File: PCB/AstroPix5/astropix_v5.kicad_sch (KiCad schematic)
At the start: 40 parts, among them J1 HBOut, J12 Measures_Analog, J13 pcie_GECCO, J14 Bias, J2 Conn_01x05, J4 HBOut, J5 HBOut, J7 HV_in_external, J8 Conn_01x03, U2 AstroPix5_split_powerring

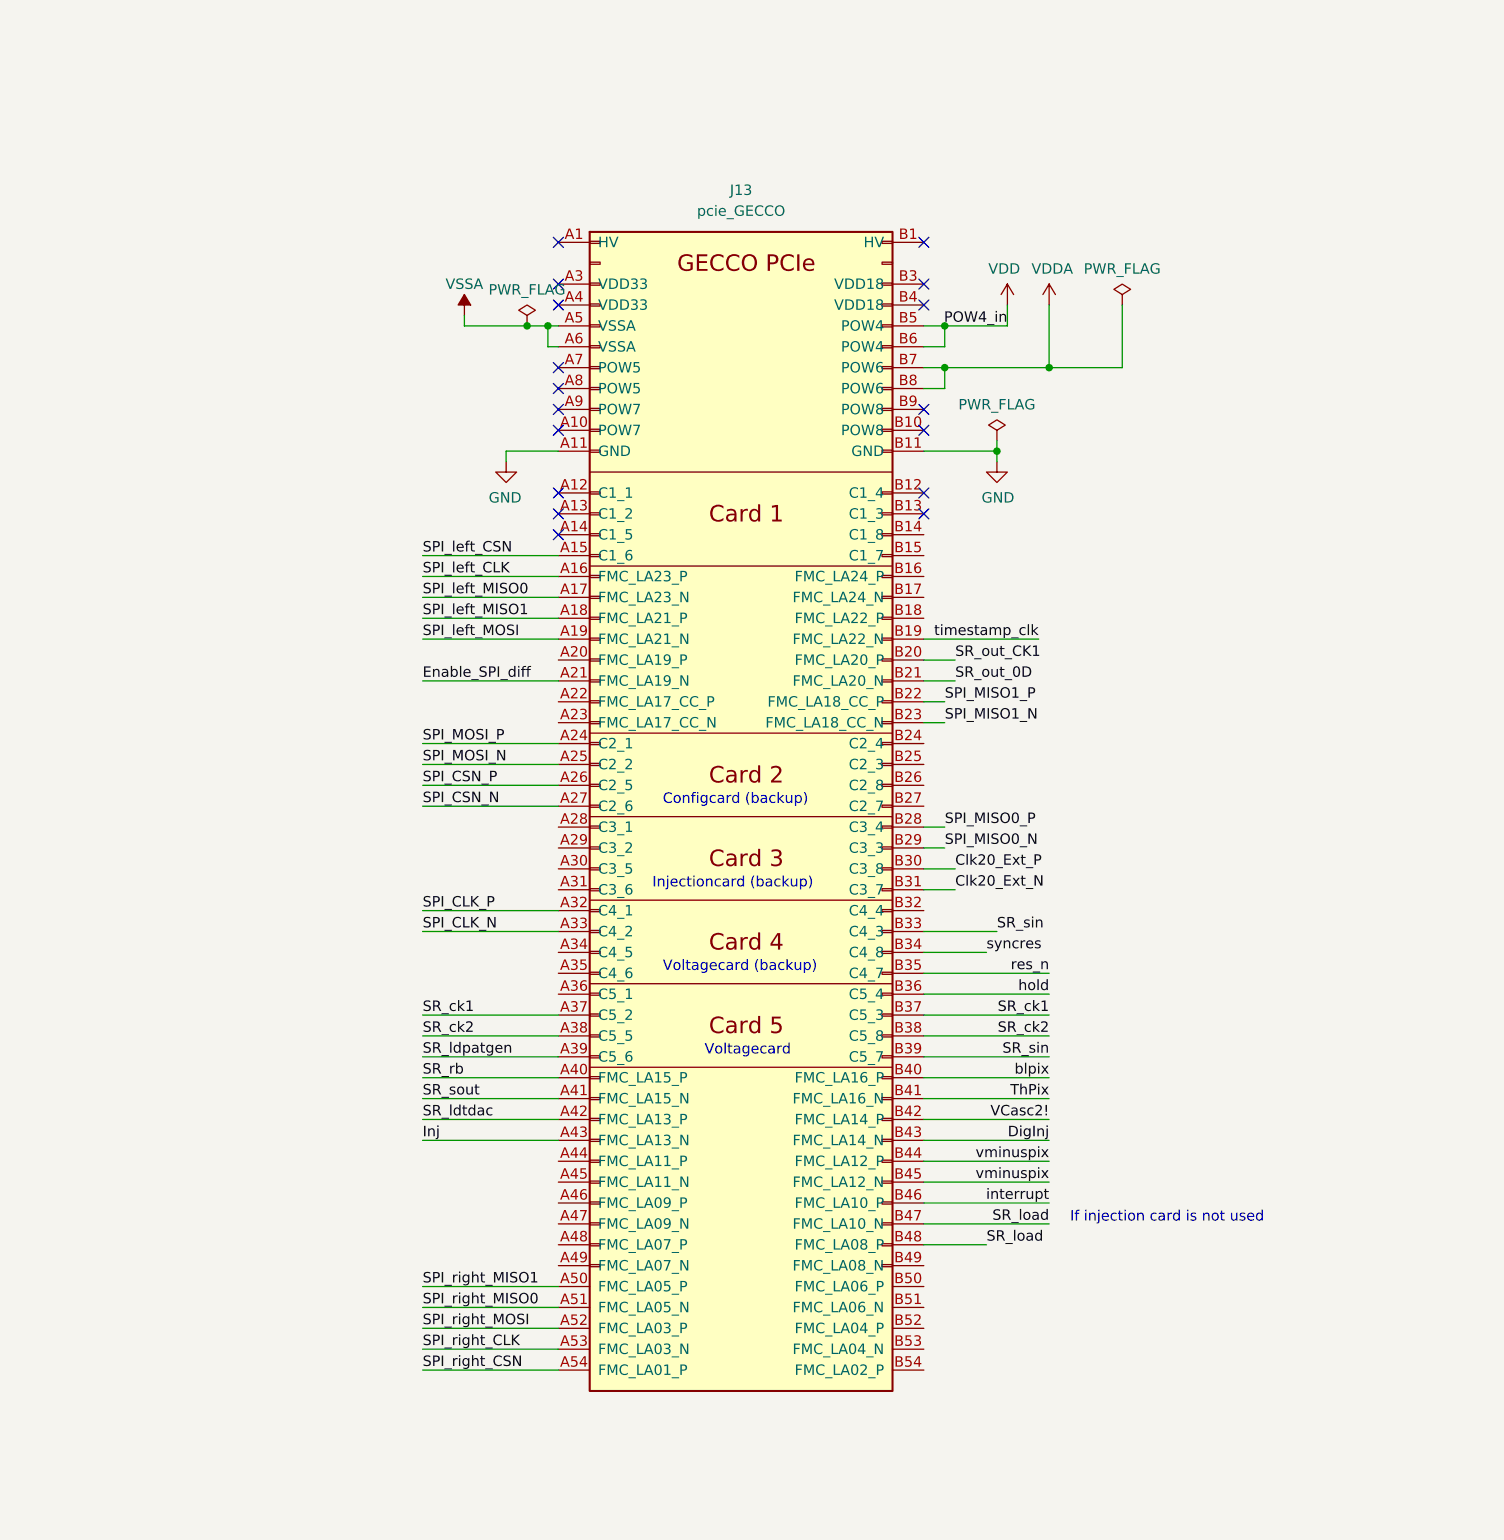
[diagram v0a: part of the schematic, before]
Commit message: Gecco schematic changes and new fan out layout routing
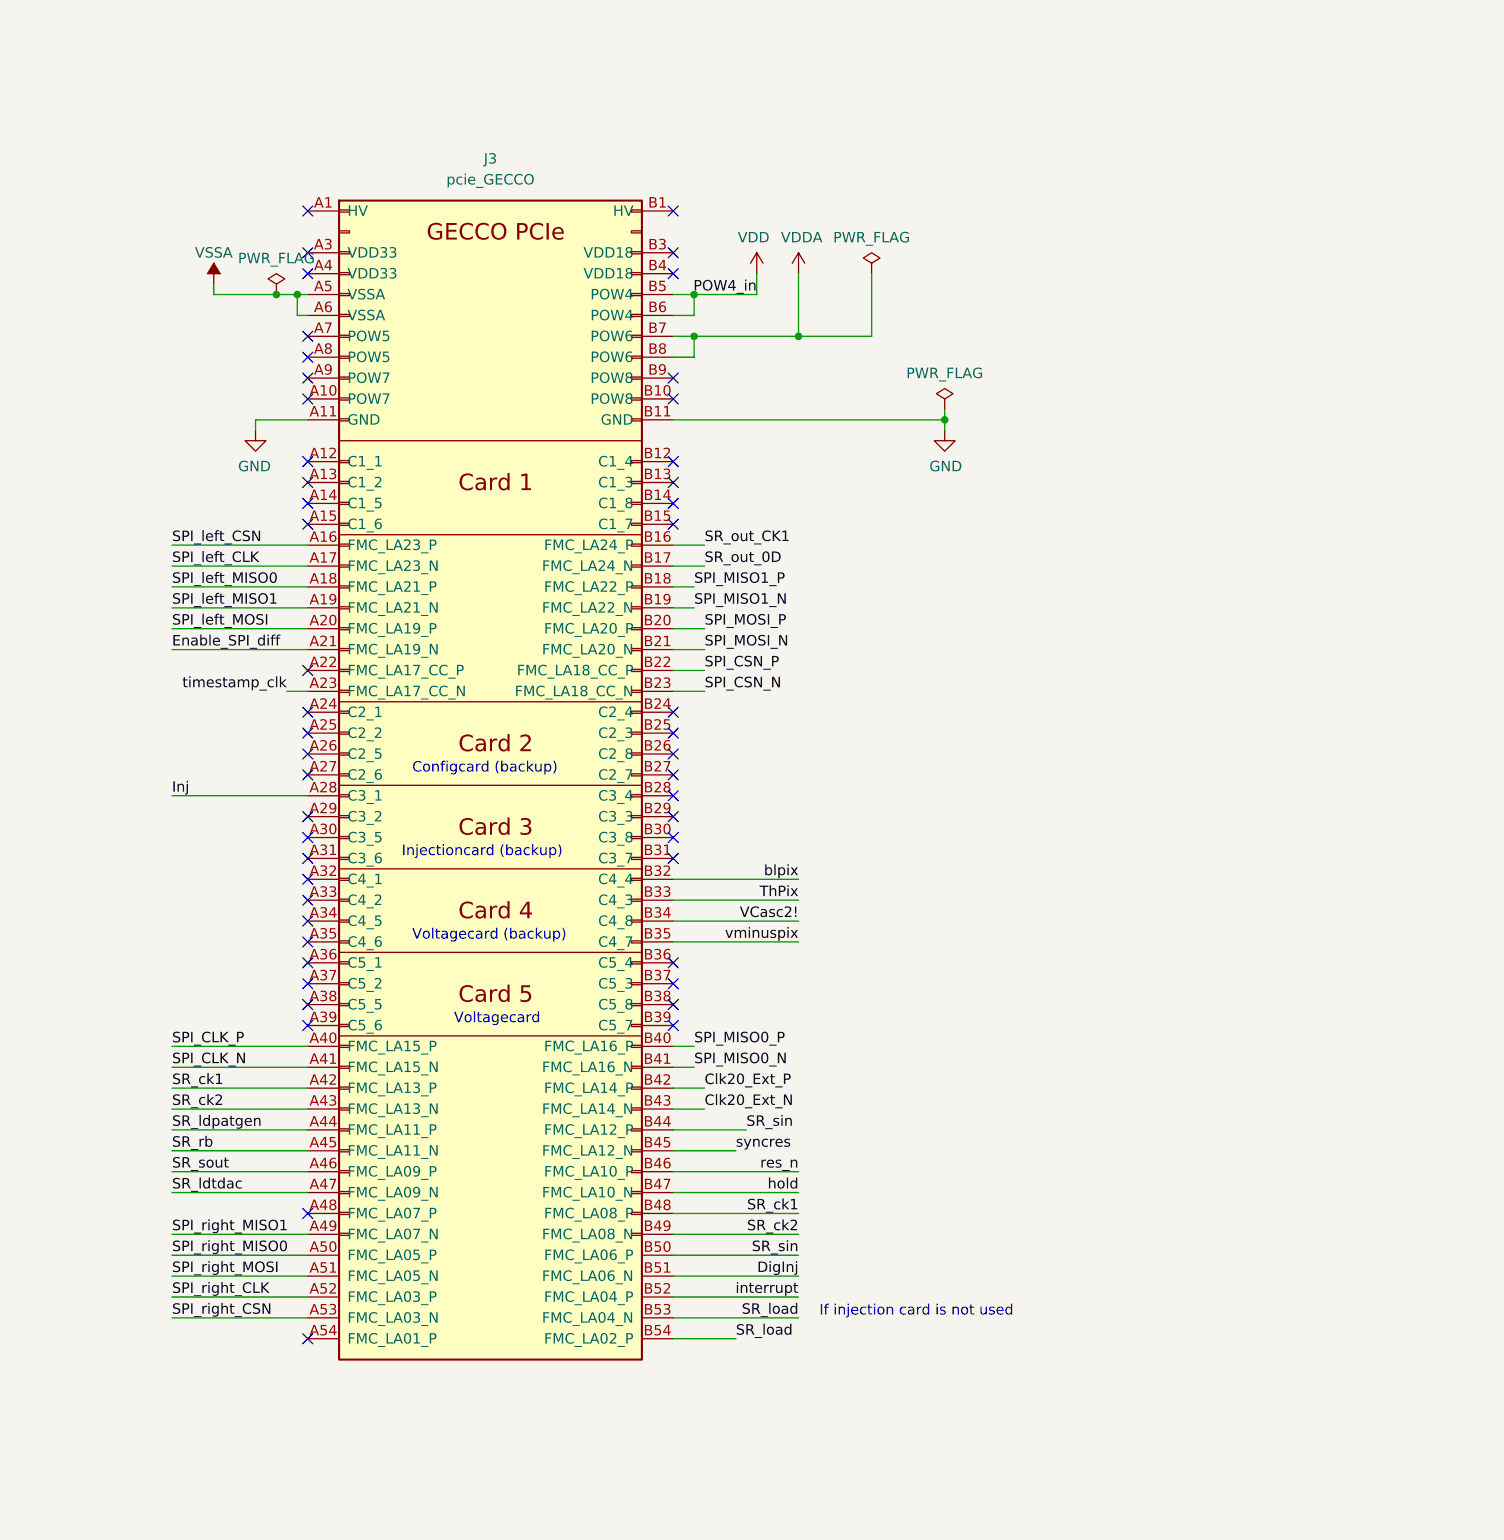
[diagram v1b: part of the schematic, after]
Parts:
- removed J13: pcie_GECCO, Connector_PCBEdge:BUS_PCIexpress_x16, symbol astropix:pcie_GECCO_v2
- added J3: pcie_GECCO, Connector_PCBEdge:BUS_PCIexpress_x16, symbol astropix:pcie_GECCO_v2
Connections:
- net Clk20_Ext_N: now also J3.B43 (FMC_LA14_N)
- net Clk20_Ext_P: now also J3.B42 (FMC_LA14_P)
- net DigInj: now also J3.B51 (FMC_LA06_N)
- net Enable_SPI_diff: now also J3.A21 (FMC_LA19_N)
- net GND: now also J3.A11 (GND), J3.B11 (GND)
- net Inj: now also J3.A28 (C3_1)
- net SPI_CLK_N: now also J3.A41 (FMC_LA15_N)
- net SPI_CLK_P: now also J3.A40 (FMC_LA15_P)
- net SPI_CSN_N: now also J3.B23 (FMC_LA18_CC_N)
- net SPI_CSN_P: now also J3.B22 (FMC_LA18_CC_P)
- net SPI_MISO0_N: now also J3.B41 (FMC_LA16_N)
- net SPI_MISO0_P: now also J3.B40 (FMC_LA16_P)
- net SPI_MISO1_N: now also J3.B19 (FMC_LA22_N)
- net SPI_MISO1_P: now also J3.B18 (FMC_LA22_P)
- net SPI_MOSI_N: now also J3.B21 (FMC_LA20_N)
- net SPI_MOSI_P: now also J3.B20 (FMC_LA20_P)
- net SPI_left_CLK: now also J3.A17 (FMC_LA23_N)
- net SPI_left_CSN: now also J3.A16 (FMC_LA23_P)
- net SPI_left_MISO0: now also J3.A18 (FMC_LA21_P)
- net SPI_left_MISO1: now also J3.A19 (FMC_LA21_N)
- net SPI_left_MOSI: now also J3.A20 (FMC_LA19_P)
- net SPI_right_CLK: now also J3.A52 (FMC_LA03_P)
- net SPI_right_CSN: now also J3.A53 (FMC_LA03_N)
- net SPI_right_MISO0: now also J3.A50 (FMC_LA05_P)
- net SPI_right_MISO1: now also J3.A49 (FMC_LA07_N)
- net SPI_right_MOSI: now also J3.A51 (FMC_LA05_N)
- net SR_ck1: now also J3.A42 (FMC_LA13_P), J3.B48 (FMC_LA08_P)
- net SR_ck2: now also J3.A43 (FMC_LA13_N), J3.B49 (FMC_LA08_N)
- net SR_ldpatgen: now also J3.A44 (FMC_LA11_P)
- net SR_ldtdac: now also J3.A47 (FMC_LA09_N)
- net SR_load: now also J3.B53 (FMC_LA04_N), J3.B54 (FMC_LA02_P)
- net SR_out_0D: now also J3.B17 (FMC_LA24_N)
- net SR_out_CK1: now also J3.B16 (FMC_LA24_P)
- net SR_rb: now also J3.A45 (FMC_LA11_N)
- net SR_sin: now also J3.B44 (FMC_LA12_P), J3.B50 (FMC_LA06_P)
- net SR_sout: now also J3.A46 (FMC_LA09_P)
- net ThPix: now also J3.B33 (C4_3)
- net VCasc2!: now also J3.B34 (C4_8)
- net VDD: now also J3.B5 (POW4), J3.B6 (POW4)
- net VDDA: now also J3.B7 (POW6), J3.B8 (POW6)
- net VSSA: now also J3.A5 (VSSA), J3.A6 (VSSA)
- net blpix: now also J3.B32 (C4_4)
- net hold: now also J3.B47 (FMC_LA10_N)
- net interrupt: now also J3.B52 (FMC_LA04_P)
- net res_n: now also J3.B46 (FMC_LA10_P)
- net syncres: now also J3.B45 (FMC_LA12_N)
- net timestamp_clk: now also J3.A23 (FMC_LA17_CC_N)
- net vminuspix: now also J3.B35 (C4_7)
- no-connect marks 21 -> 54
